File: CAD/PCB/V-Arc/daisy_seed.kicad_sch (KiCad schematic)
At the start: 21 parts, among them SW2 SW_SPDT, SW3 SW_SPDT, SW4 SW_SPDT, SW5 SW_SPDT, SW6 SW_SPDT, SW7 SW_Push, SW8 SW_SPDT_MSM, SW9 SW_SPDT, U6 Daisy_Seed

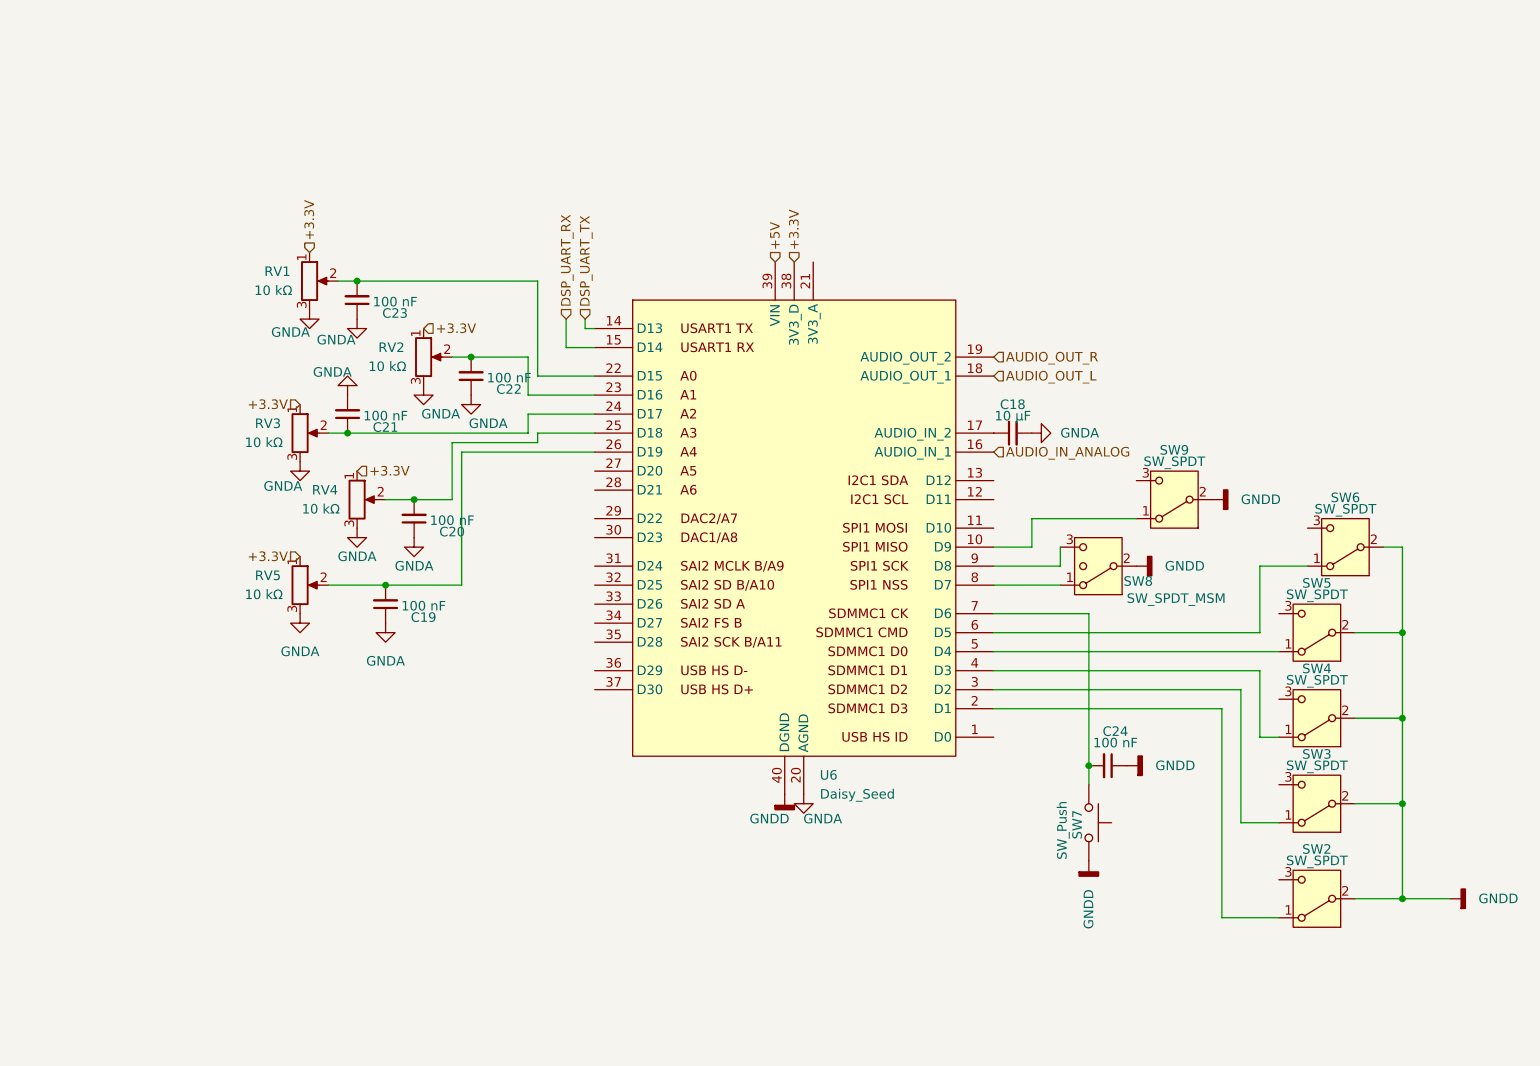
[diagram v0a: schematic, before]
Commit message: Added a sheet and organized
-Added XIAO ESP32 Core sheet
-Titled all sheets
-Added power switch to the power sheet
-Organized all sheets with text boxes
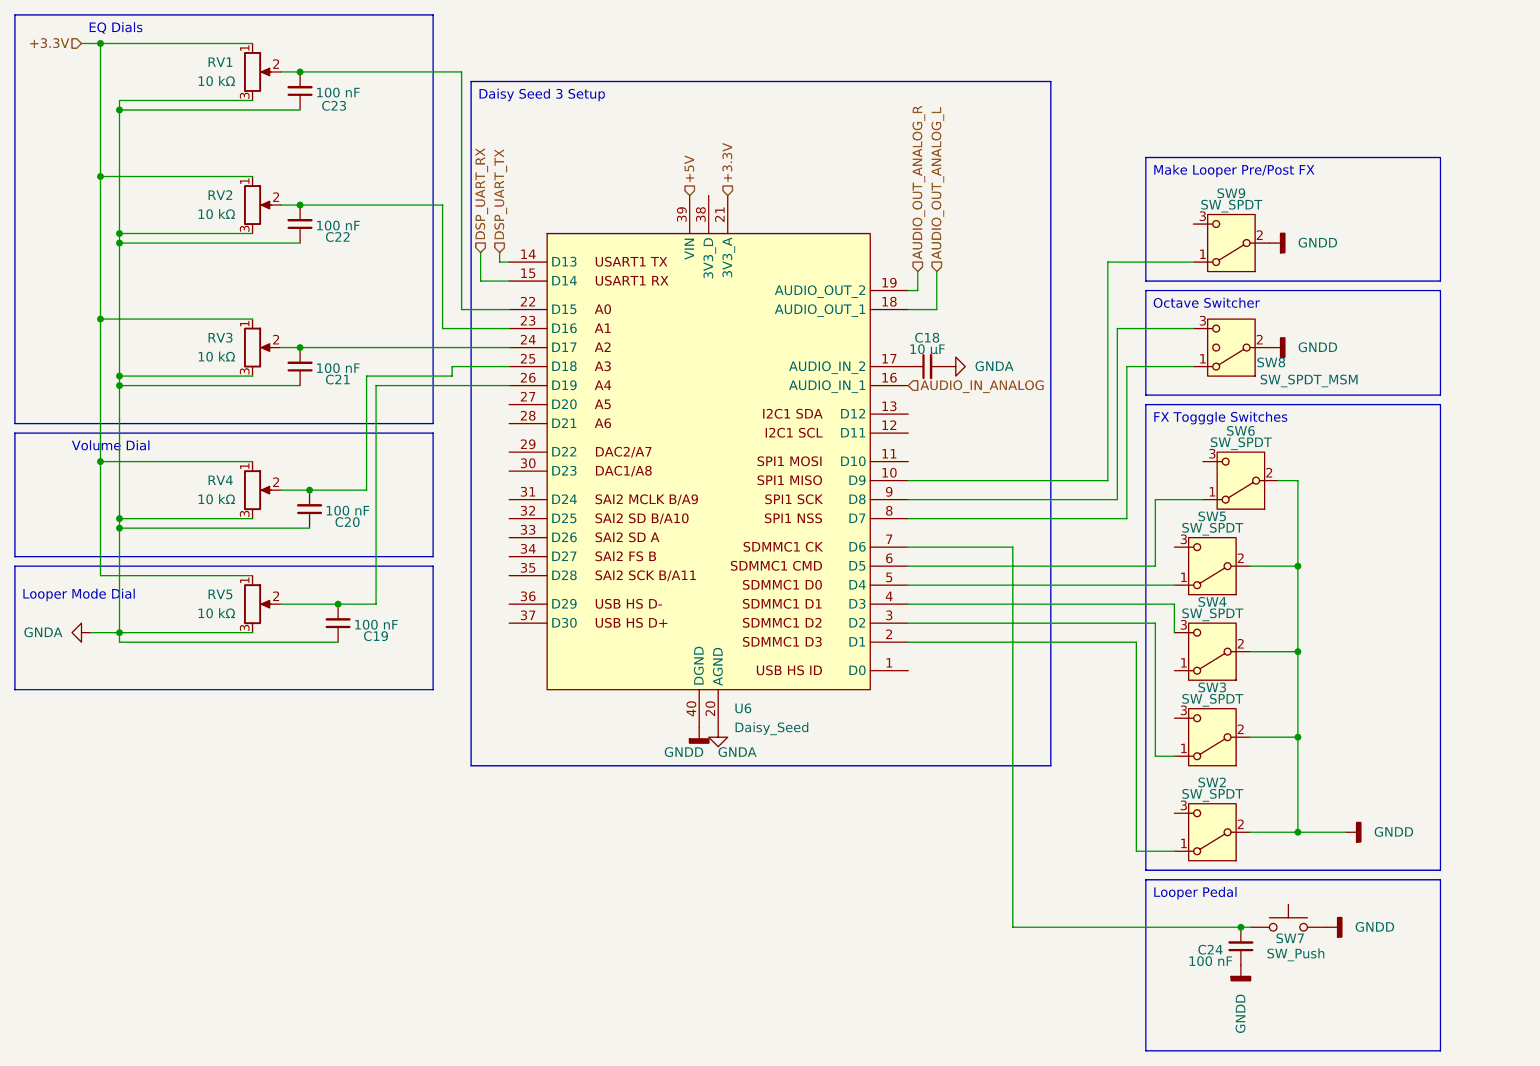
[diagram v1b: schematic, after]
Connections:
- net +3.3V: now also U6.21 (3V3_A); no longer U6.38 (3V3_D)
- net GNDA: now also C21.1; no longer C21.2
- net at SW4.1 (A): no longer U6.4 (D3)
- net at SW4.3 (C): now also U6.4 (D3)
- net at RV3.2, U6.24 (D17): now also C21.2; no longer C21.1
- net AUDIO_OUT_L renamed AUDIO_OUT_ANALOG_L
- net AUDIO_OUT_R renamed AUDIO_OUT_ANALOG_R
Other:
- title: (none) -> V-Arc Daisy Seed 3 Core
- moved on the sheet: C18, C19, C20, C21, C22, C23, C24, RV1, RV2, RV3, RV4, RV5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
